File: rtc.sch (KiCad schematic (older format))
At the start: 16 parts, among them U36 74LS05, U9 MSM6242B, Y9 32768 Hz

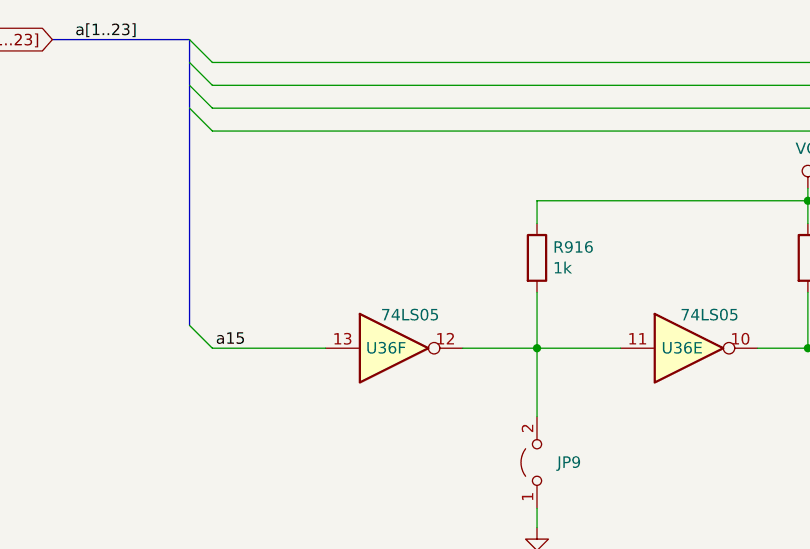
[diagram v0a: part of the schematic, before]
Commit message: Add trapdoor connector
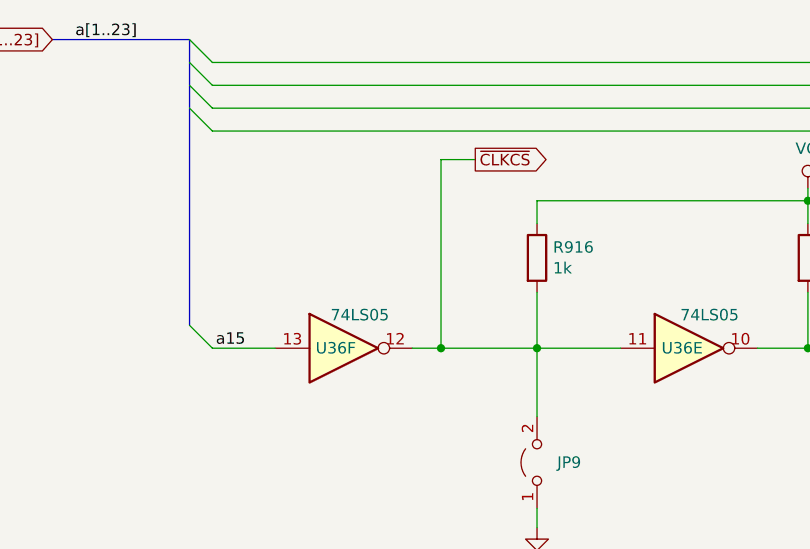
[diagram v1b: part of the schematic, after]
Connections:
- net ~CLKCS: now reaches JP9.2 (B), R916.2, U36.11, U36.12
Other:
- moved on the sheet: U36F
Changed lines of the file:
@@
 $Descr A4 11693 8268
 encoding utf-8
-Sheet 13 13
+Sheet 13 14
 Title "Rämixx500"
 Date "2019-04-23"
@@
 	2595 2525 2495 2425
 Wire Wire Line
-	2595 2525 3090 2525
+	2595 2525 2870 2525
 Text Label 2610 2525 0    50   ~ 0
 a15
@@
 L 74xx:74LS05 U36
 U 6 1 5CF8B8D2
-P 3390 2525
-F 0 "U36" H 3355 2525 50  0000 C CNN
-F 1 "74LS05" H 3460 2670 50  0000 C CNN
-F 2 "Package_DIP:DIP-14_W7.62mm_Socket_LongPads" H 3390 2525 50  0001 C CNN
-F 3 "http://www.ti.com/lit/gpn/sn74LS05" H 3390 2525 50  0001 C CNN
-	6    3390 2525
-	1    0    0    -1
-$EndComp
-Wire Wire Line
-	3690 2525 4015 2525
+P 3170 2525
+F 0 "U36" H 3135 2525 50  0000 C CNN
+F 1 "74LS05" H 3240 2670 50  0000 C CNN
+F 2 "Package_DIP:DIP-14_W7.62mm_Socket_LongPads" H 3170 2525 50  0001 C CNN
+F 3 "http://www.ti.com/lit/gpn/sn74LS05" H 3170 2525 50  0001 C CNN
+	6    3170 2525
+	1    0    0    -1
+$EndComp
 Wire Wire Line
 	2595 1275 7245 1275
@@
 Text Notes 3170 5025 2    50   ~ 0
 This diode replaces R913 on the original schematics\nso that we can use a non-rechargeable battery. Use\na Schottky diode to minimize the voltage drop.
+Wire Wire Line
+	3470 2525 3595 2525
+Wire Wire Line
+	3595 2525 3595 1700
+Wire Wire Line
+	3595 1700 3745 1700
+Text GLabel 3745 1700 2    50   Output ~ 0
+~CLKCS
+Connection ~ 3595 2525
+Wire Wire Line
+	3595 2525 4015 2525
 Wire Bus Line
 	6845 1675 6845 1975

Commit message: Fix power-up reset
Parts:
- C9, C911: footprint (none) -> Raemixx500:C_Axial_L6.3mm_D2.5mm_P10.16mm
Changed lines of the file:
@@
 EESchema Schematic File Version 4
 LIBS:Raemix500-cache
-EELAYER 26 0
+EELAYER 29 0
 EELAYER END
 $Descr A4 11693 8268
@@
 F 0 "C911" V 9505 2725 50  0000 C CNN
 F 1 "22p" V 9785 2725 50  0000 C CNN
-F 2 "" H 9678 2575 50  0001 C CNN
+F 2 "Raemixx500:C_Axial_L6.3mm_D2.5mm_P10.16mm" H 9678 2575 50  0001 C CNN
 F 3 "~" H 9640 2725 50  0001 C CNN
 	1    9640 2725
@@
 F 0 "C9" H 5605 5866 50  0000 L CNN
 F 1 "330n" H 5605 5775 50  0000 L CNN
-F 2 "" H 5528 5670 50  0001 C CNN
+F 2 "Raemixx500:C_Axial_L6.3mm_D2.5mm_P10.16mm" H 5528 5670 50  0001 C CNN
 F 3 "~" H 5490 5820 50  0001 C CNN
 	1    5490 5820

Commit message: Top layer done!
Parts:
- TC9: footprint (none) -> Raemixx500:VariCap
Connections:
- net GND: now also TC9.2; no longer TC9.1
- net at U9.16 (XT), Y9.1: now also TC9.1; no longer TC9.2
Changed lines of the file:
@@
 U 1 1 5CF819AD
 P 9640 2325
-F 0 "TC9" V 9388 2325 50  0000 C CNN
-F 1 "6.8-45p" V 9479 2325 50  0000 C CNN
-F 2 "" H 9640 2325 50  0001 C CNN
+F 0 "TC9" V 9892 2325 50  0000 C CNN
+F 1 "6.8-45p" V 9801 2325 50  0000 C CNN
+F 2 "Raemixx500:VariCap" H 9640 2325 50  0001 C CNN
 F 3 "~" H 9640 2325 50  0001 C CNN
 	1    9640 2325
-	0    1    1    0
+	0    -1   -1   0
 $EndComp
 $Comp

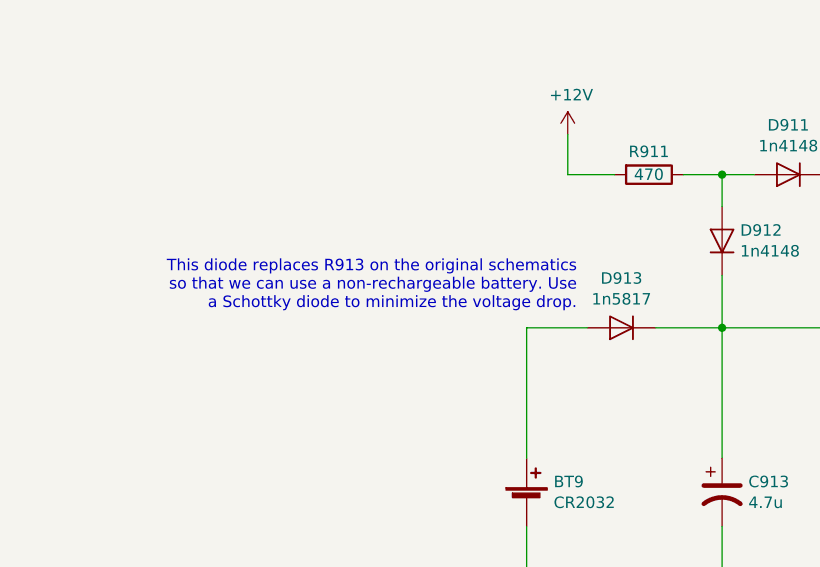
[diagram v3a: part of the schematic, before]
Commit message: Fix a lot of ERC/DRC errors
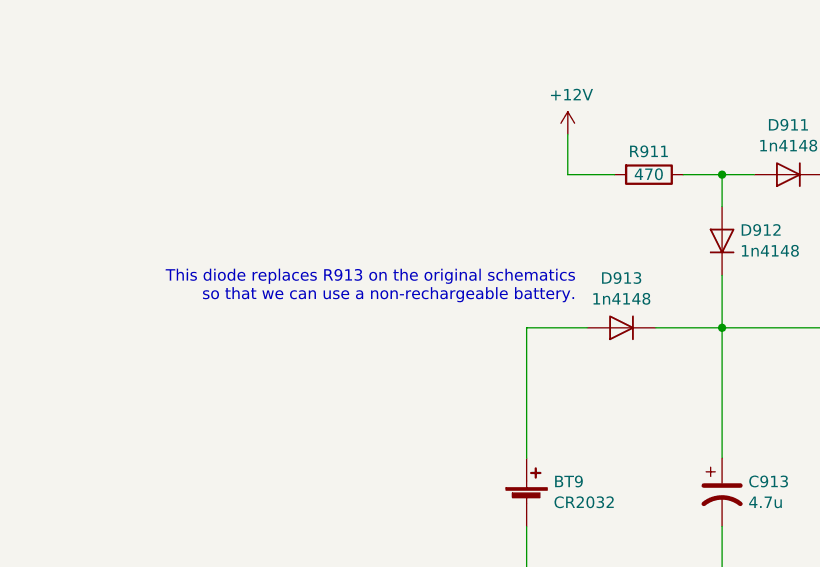
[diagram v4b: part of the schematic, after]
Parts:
- D913: value 1n5817 -> 1n4148
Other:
- note added: "This diode replaces R913 on the original schematics\nso that we can use a non-rechargeable battery."
- note removed: "This diode replaces R913 on the original schematics\nso that we can use a non-rechargeable battery. Use\na Schottky diode to minimize the voltage drop."
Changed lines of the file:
@@
 EESchema Schematic File Version 4
-LIBS:Raemix500-cache
-EELAYER 29 0
+EELAYER 30 0
 EELAYER END
 $Descr A4 11693 8268
@@
 P 3365 5100
 F 0 "D913" H 3365 4884 50  0000 C CNN
-F 1 "1n5817" H 3365 4975 50  0000 C CNN
+F 1 "1n4148" H 3365 4975 50  0000 C CNN
 F 2 "Diode_THT:D_DO-41_SOD81_P12.70mm_Horizontal" H 3365 5100 50  0001 C CNN
 F 3 "~" H 3365 5100 50  0001 C CNN
@@
 	-1   0    0    1
 $EndComp
-Text Notes 3170 5025 2    50   ~ 0
-This diode replaces R913 on the original schematics\nso that we can use a non-rechargeable battery. Use\na Schottky diode to minimize the voltage drop.
+Text Notes 3165 4990 2    50   ~ 0
+This diode replaces R913 on the original schematics\nso that we can use a non-rechargeable battery.
 Wire Wire Line
 	3470 2525 3595 2525

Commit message: Switch back to SOD27 footprint for D913
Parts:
- D913: footprint Diode_THT:D_DO-41_SOD81_P12.70mm_Horizontal -> Diode_THT:D_DO-35_SOD27_P12.70mm_Horizontal
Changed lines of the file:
@@
 F 0 "D913" H 3365 4884 50  0000 C CNN
 F 1 "1n4148" H 3365 4975 50  0000 C CNN
-F 2 "Diode_THT:D_DO-41_SOD81_P12.70mm_Horizontal" H 3365 5100 50  0001 C CNN
+F 2 "Diode_THT:D_DO-35_SOD27_P12.70mm_Horizontal" H 3365 5100 50  0001 C CNN
 F 3 "~" H 3365 5100 50  0001 C CNN
 	1    3365 5100
